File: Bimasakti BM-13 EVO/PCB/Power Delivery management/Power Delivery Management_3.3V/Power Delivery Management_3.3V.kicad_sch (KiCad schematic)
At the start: 27 parts, among them J1 +12V In, J2 Slow Start, J3 Conn_01x03_Socket

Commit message: pdm
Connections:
- net +12V: now also J1.1 (Pin_1)
- net GND: now also J1.2 (Pin_2)
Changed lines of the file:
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@@
+	(wire
+		(pts
+			(xy 31.75 38.1) (xy 33.02 38.1)
+		)
+		(stroke
+			(width 0)
+			(type default)
+		)
+	)
 	(wire
 		(pts
@@
 		)
 		(stroke
+			(width 0)
+			(type default)
+		)
+	)
+	(wire
+		(pts
+			(xy 31.75 40.64) (xy 33.02 40.64)
+		)
+		(stroke

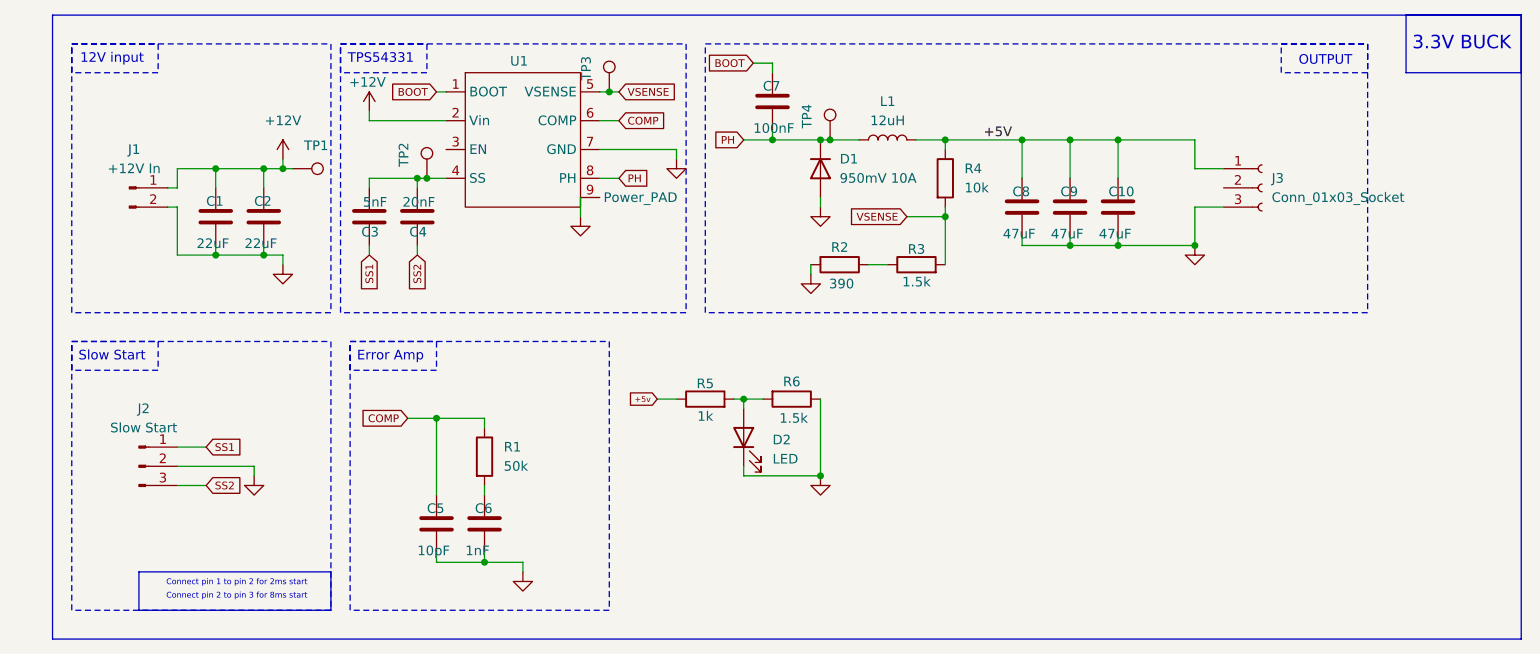
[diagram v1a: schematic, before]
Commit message: ganti value dan layout
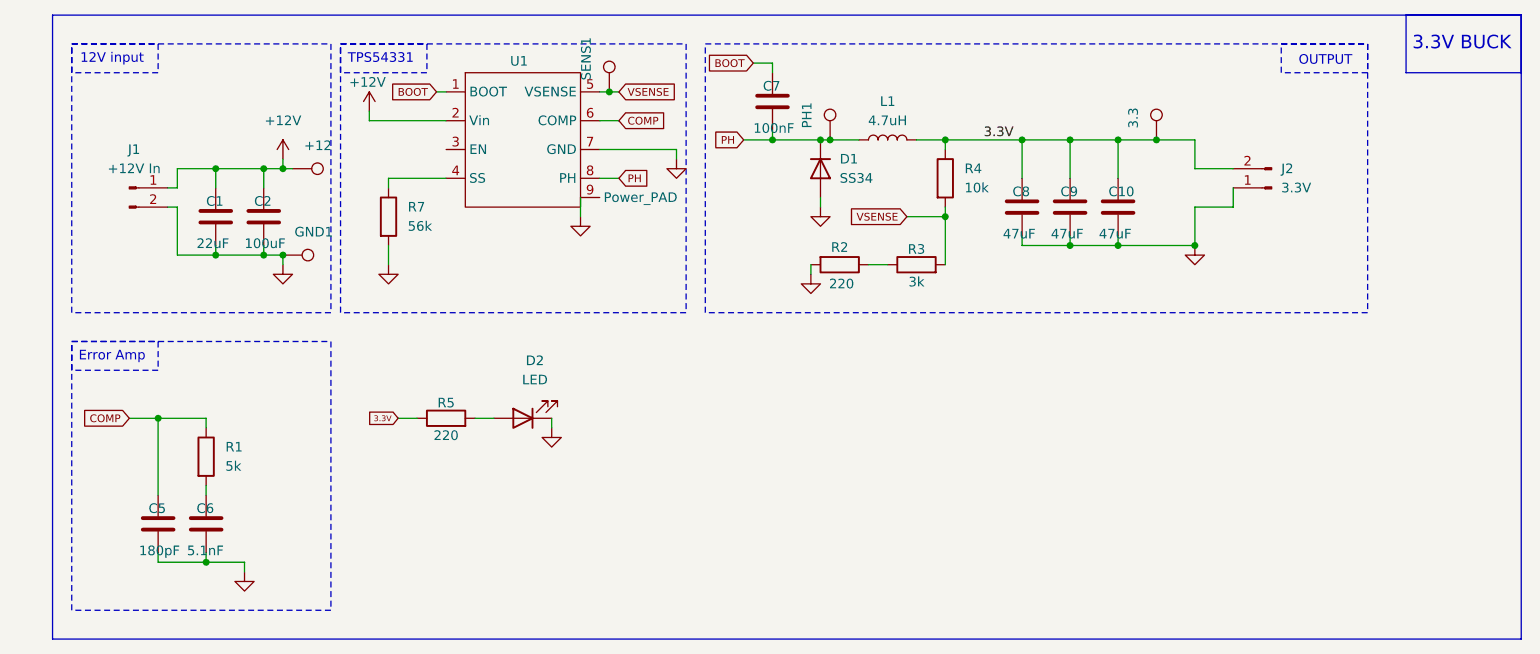
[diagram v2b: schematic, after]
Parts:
- removed C3: 5nF, Capacitor_SMD:C_0603_1608Metric, symbol Device:C
- removed C4: 20nF, Capacitor_SMD:C_0603_1608Metric, symbol Device:C
- removed J2: Slow Start, Connector_PinHeader_2.54mm:PinHeader_1x03_P2.54mm_Vertical, symbol Connector:Conn_01x03_Pin
- removed J3: Conn_01x03_Socket, Connector_JST:JST_EH_B3B-EH-A_1x03_P2.50mm_Vertical, symbol Connector:Conn_01x03_Socket
- removed R6: 1.5k, Resistor_SMD:R_0603_1608Metric, symbol Device:R
- removed TP2: TestPoint, TestPoint:TestPoint_Keystone_5015_Micro-Minature, symbol Connector:TestPoint
- added 3.3, GND1: TestPoint, TestPoint:TestPoint_Bridge_Pitch2.0mm_Drill0.7mm, symbol Connector:TestPoint
- added J2: 3.3V, Connector_JST:JST_EH_B2B-EH-A_1x02_P2.50mm_Vertical, symbol Connector:Conn_01x02_Pin
- added R7: 56k, Resistor_SMD:R_0603_1608Metric, symbol Device:R
- +12: renamed from TP1; footprint TestPoint:TestPoint_Keystone_5015_Micro-Minature -> TestPoint:TestPoint_Bridge_Pitch2.0mm_Drill0.7mm
- C2: value 22uF -> 100uF
- C5: value 10pF -> 180pF
- C6: value 1nF -> 5.1nF
- D1: value 950mV 10A -> SS34; footprint Package_TO_SOT_THT:TO-251-2_Vertical -> Diode_SMD:D_SMA
- L1: value 12uH -> 4.7uH
- PH1: renamed from TP4; footprint TestPoint:TestPoint_Keystone_5015_Micro-Minature -> TestPoint:TestPoint_Bridge_Pitch2.0mm_Drill0.7mm
- R1: value 50k -> 5k
- R2: value 390 -> 220
- R3: value 1.5k -> 3k
- R5: value 1k -> 220
- SENS1: renamed from TP3; footprint TestPoint:TestPoint_Keystone_5015_Micro-Minature -> TestPoint:TestPoint_Bridge_Pitch2.0mm_Drill0.7mm
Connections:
- net +5v is gone; now on net 3.3V: R5.1
- net GND: now also GND1.1, J2.1 (Pin_1), R7.2
- net at U1.4 (SS): now also R7.1
- net +5V renamed 3.3V
- net 3.3V: now also 3.3.1, J2.2 (Pin_2)
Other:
- note removed: "Connect pin 1 to pin 2 for 2ms start"
- note removed: "Connect pin 2 to pin 3 for 8ms start"
- note removed: "Slow Start"
- moved on the sheet: C5, C6, D2, R1, R5

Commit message: pdm finishing tambah logo
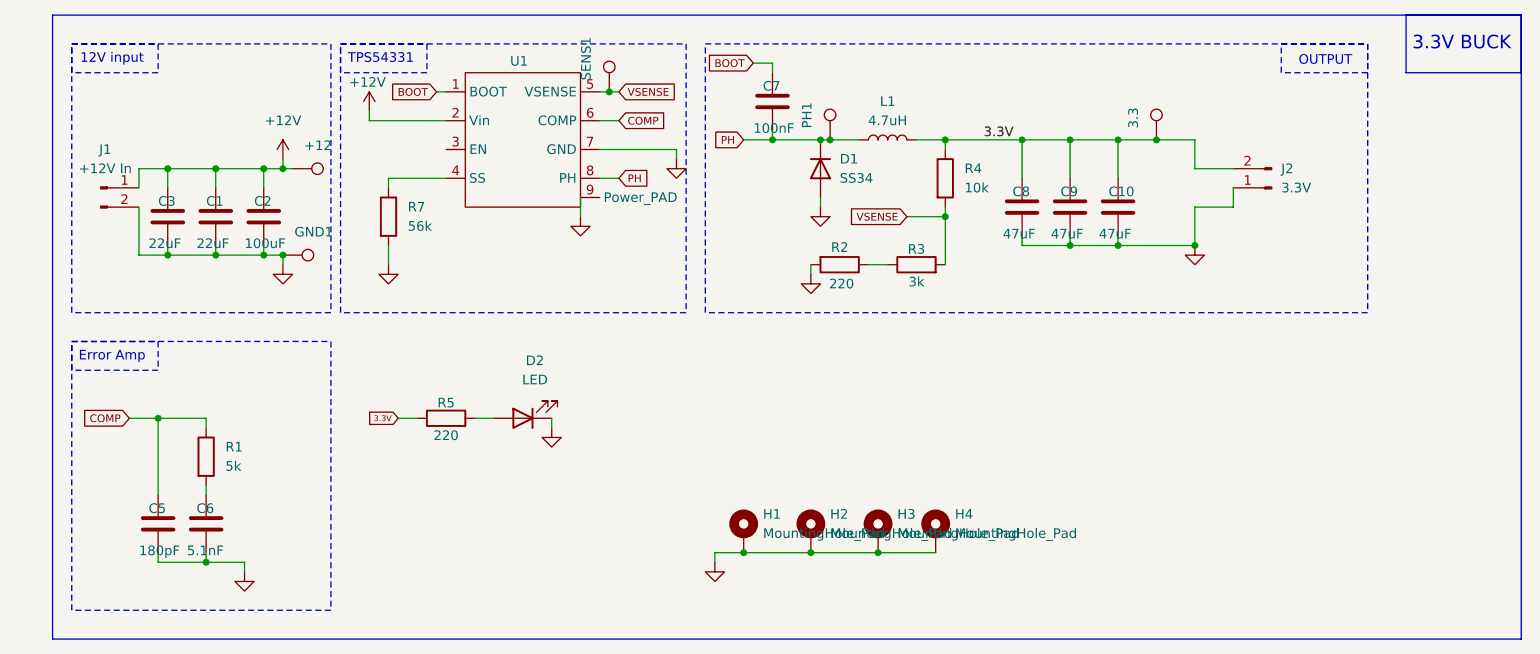
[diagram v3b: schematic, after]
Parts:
- added C3: 22uF, Capacitor_SMD:C_1210_3225Metric, symbol Device:C
- added H1, H2, H3, H4: MountingHole_Pad, MountingHole:MountingHole_3.2mm_M3_Pad_TopBottom, symbol Mechanical:MountingHole_Pad
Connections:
- net +12V: now also C3.1
- net GND: now also C3.2, H1.1, H2.1, H3.1, H4.1
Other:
- moved on the sheet: J1

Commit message: ngecilin pdm
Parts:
- removed H1, H2, H3, H4: MountingHole_Pad, MountingHole:MountingHole_3.2mm_M3_Pad_TopBottom, symbol Mechanical:MountingHole_Pad
- removed J1: +12V In, Connector_JST:JST_EH_B2B-EH-A_1x02_P2.50mm_Vertical, symbol Connector:Conn_01x02_Pin
- removed J2: 3.3V, Connector_JST:JST_EH_B2B-EH-A_1x02_P2.50mm_Vertical, symbol Connector:Conn_01x02_Pin
- added J3, J4: Conn_01x10_Socket, Connector_PinHeader_2.54mm:PinHeader_1x10_P2.54mm_Vertical, symbol Connector:Conn_01x10_Socket
- L1: footprint Inductor_SMD:L_Coilcraft_MSS1278T-XXX -> Inductor_SMD:L_Changjiang_FNR5020S
- R5: value 220 -> 2k
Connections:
- net +12V: now also J3.10 (Pin_10), J3.6 (Pin_6), J3.7 (Pin_7), J3.8 (Pin_8), J3.9 (Pin_9)
- net 3.3V: now also J4.10 (Pin_10), J4.6 (Pin_6), J4.7 (Pin_7), J4.8 (Pin_8), J4.9 (Pin_9)
- net GND: now also J3.1 (Pin_1), J3.2 (Pin_2), J3.3 (Pin_3), J3.4 (Pin_4), J3.5 (Pin_5), J4.1 (Pin_1), J4.2 (Pin_2), J4.3 (Pin_3), J4.4 (Pin_4), J4.5 (Pin_5)

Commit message: pdm selesai ril, tv board sudah bagus kurang cek (mungkin ganti konektor)
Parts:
- R5: value 2k -> 500
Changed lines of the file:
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@@
 			)
 		)
-		(property "Value" "2k"
+		(property "Value" "500"
 			(at 68.58 70.866 90)
 			(effects

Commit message: buat placeholder baru dan ganti konektor
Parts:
- removed PH1: TestPoint, TestPoint:TestPoint_Bridge_Pitch2.0mm_Drill0.7mm, symbol Connector:TestPoint
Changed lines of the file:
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@@
-	)
-	(junction
-		(at 119.38 31.75)
-		(diameter 0)
-		(color 0 0 0 0)
 	)
 	(junction
@@
 	(wire
 		(pts
-			(xy 119.38 31.75) (xy 123.19 31.75)
-		)
-		(stroke
-			(width 0)
-			(type default)
-		)
-	)
-	(wire
-		(pts
-			(xy 118.11 31.75) (xy 119.38 31.75)
+			(xy 118.11 31.75) (xy 123.19 31.75)
 		)
 		(stroke
@@
 					(unit 1)
 				)
-			)
-		)
-	)
-	(symbol
-		(lib_id "Connector:TestPoint")
-		(at 119.38 31.75 0)
-		(unit 1)
-		(exclude_from_sim no)
-		(in_bom yes)
-		(on_board yes)
-		(dnp no)
-		(property "Reference" "PH1"
-			(at 116.332 30.226 90)
-			(effects
-				(font
-					(size 1.27 1.27)
-				)
-				(justify left)
-			)
-		)
-		(property "Value" "TestPoint"
-			(at 121.666 34.798 90)
-			(effects
-				(font
-					(size 1.27 1.27)
-				)
-				(justify left)
-				(hide yes)
-			)
-		)
-		(property "Footprint" "TestPoint:TestPoint_Bridge_Pitch2.0mm_Drill0.7mm"
-			(at 124.46 31.75 0)
-			(effects
-				(font
-					(size 1.27 1.27)
-				)
-				(hide yes)
-			)
-		)
-		(property "Datasheet" "~"
-			(at 124.46 31.75 0)
-			(effects
-				(font
-					(size 1.27 1.27)
-				)
-				(hide yes)
-			)
-		)
-		(property "Description" "test point"
-			(at 119.38 31.75 0)
-			(effects
-				(font
-					(size 1.27 1.27)
-				)
-				(hide yes)
-			)
-		)
-		(pin "1"
-		)
-		(instances
-			(project "Power Delivery Management_3.3V"
-				(path "/af22792e-0541-4d5c-a586-5d132a154483"
-					(reference "PH1")
-					(unit 1)
-				)

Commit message: tambah i2c di tele
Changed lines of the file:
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@@
+	(wire
+		(pts
+			(xy 90.17 39.37) (xy 86.36 39.37)
+		)
+		(stroke
+			(width 0)
+			(type default)
+		)
+	)
+	(wire
+		(pts
+			(xy 90.17 39.37) (xy 90.17 41.91)
+		)
+		(stroke
+			(width 0)
+			(type default)
+		)
+	)
 	(wire
 		(pts
@@
 		(pts
 			(xy 118.11 39.37) (xy 118.11 40.64)
-		)
-		(stroke
-			(width 0)
-			(type default)
-		)
-	)
-	(wire
-		(pts
-			(xy 86.36 39.37) (xy 86.36 41.91)
 		)
 		(stroke
@@
 	(symbol
 		(lib_id "power:GND")
-		(at 86.36 41.91 0)
+		(at 90.17 41.91 0)
 		(unit 1)
 		(exclude_from_sim no)
@@
 		(fields_autoplaced yes)
 		(property "Reference" "#PWR06"
-			(at 86.36 48.26 0)
+			(at 90.17 48.26 0)
 			(effects
 				(font
@@
 		)
 		(property "Value" "GND"
-			(at 86.36 46.99 0)
+			(at 90.17 46.99 0)
 			(effects
 				(font
@@
 		)
 		(property "Footprint" ""
-			(at 86.36 41.91 0)
+			(at 90.17 41.91 0)
 			(effects
 				(font
@@
 		)
 		(property "Datasheet" ""
-			(at 86.36 41.91 0)
+			(at 90.17 41.91 0)
 			(effects
 				(font
@@
 		)
 		(property "Description" "Power symbol creates a global label with name \"GND\" , ground"
-			(at 86.36 41.91 0)
-			(effects
-				(font
+			(at 90.17 41.91 0)
+			(effects
+				(font
